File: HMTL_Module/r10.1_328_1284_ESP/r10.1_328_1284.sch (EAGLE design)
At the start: 47 parts, among them U2 ATMEGA328P_PDIP, Y1 16MHz

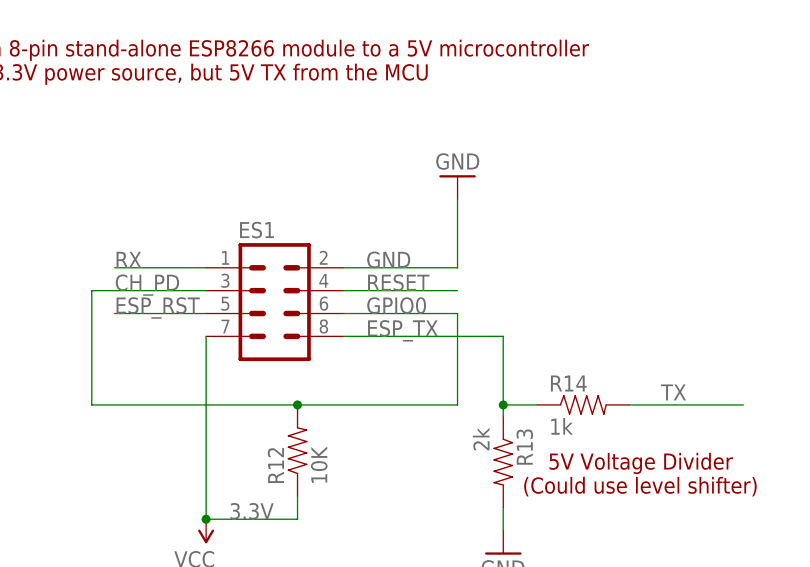
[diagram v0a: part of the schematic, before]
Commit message: Finished adding ESP to HMTL r10.1
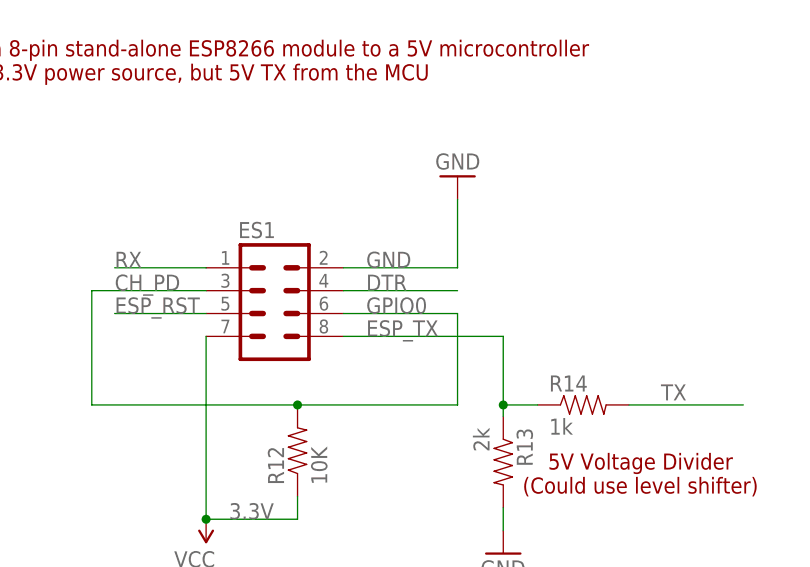
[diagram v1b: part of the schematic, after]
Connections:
- net DTR: now also ES1.4
- net RESET: no longer ES1.4
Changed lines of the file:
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@@
 <label x="88.9" y="114.3" size="1.778" layer="95"/>
+</segment>
+<segment>
+<pinref part="ES1" gate="G$1" pin="4"/>
+<wire x1="271.78" y1="66.04" x2="284.48" y2="66.04" width="0.1524" layer="91"/>
+<label x="274.32" y="66.04" size="1.778" layer="95"/>
 </segment>
 </net>
@@
 <label x="116.84" y="71.12" size="1.778" layer="95"/>
 </segment>
-<segment>
-<pinref part="ES1" gate="G$1" pin="4"/>
-<wire x1="271.78" y1="66.04" x2="284.48" y2="66.04" width="0.1524" layer="91"/>
-<label x="274.32" y="66.04" size="1.778" layer="95"/>
-</segment>
 </net>
